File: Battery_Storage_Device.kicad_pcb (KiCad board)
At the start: 4 copper layers, 80 x 75 mm, 130 parts, among them J1 Conn_01x02_Female, J2 Conn_01x07_Male, J3 USB_B_Mini, J4 Barrel_Jack_Switch, J5 Conn_02x03_Odd_Even, K1 EE2-5NU, Q1 MMBT5551L, Q10 BSS84, Q11 BSS84, Q12 BSS138, Q13 BSS138, Q14 BSS84, Q15 BSS138, Q16 BSS84, Q17 BSS138, Q2 MMBT5551L, Q3 Q_PMOS_GDS, Q4 Q_PMOS_GDS, Q5 BSS138, Q6 BSS84, Q7 BSS84, Q8 BSS138, Q9 BSS138, U1 TLV2372, U10 ATmega328P-AU, U11 LM317_SOT-223, U2 TLV2372, U3 DG408DYZ-T, U4 DG408DYZ-T, U5 DG412xY, U6 TLV2372, U7 ADS1220xPW, U8 LM4030-4.096, U9 FT232RL, Y1 ABM3C-16.000MHZ-D4Y-T

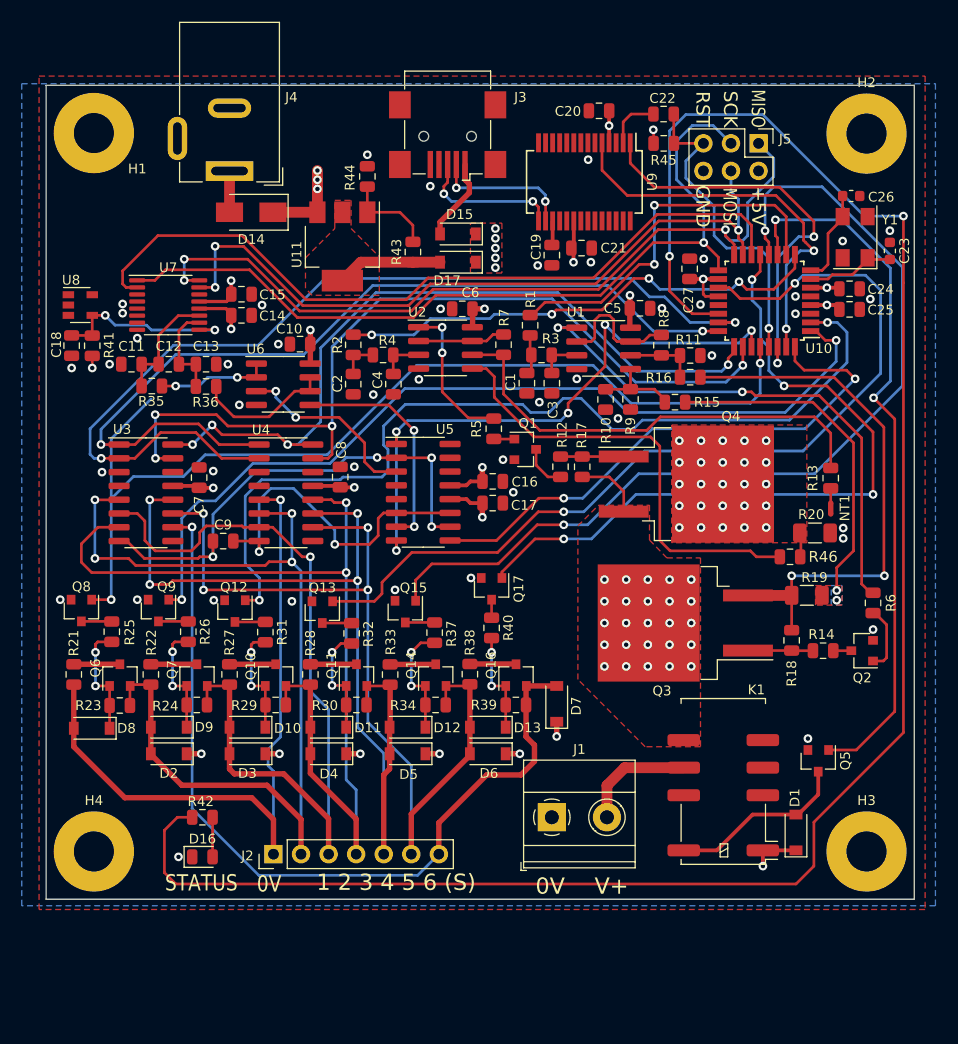
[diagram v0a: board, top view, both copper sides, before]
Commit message: Updates to the AFE power scheme to prevent discharging of the batteries
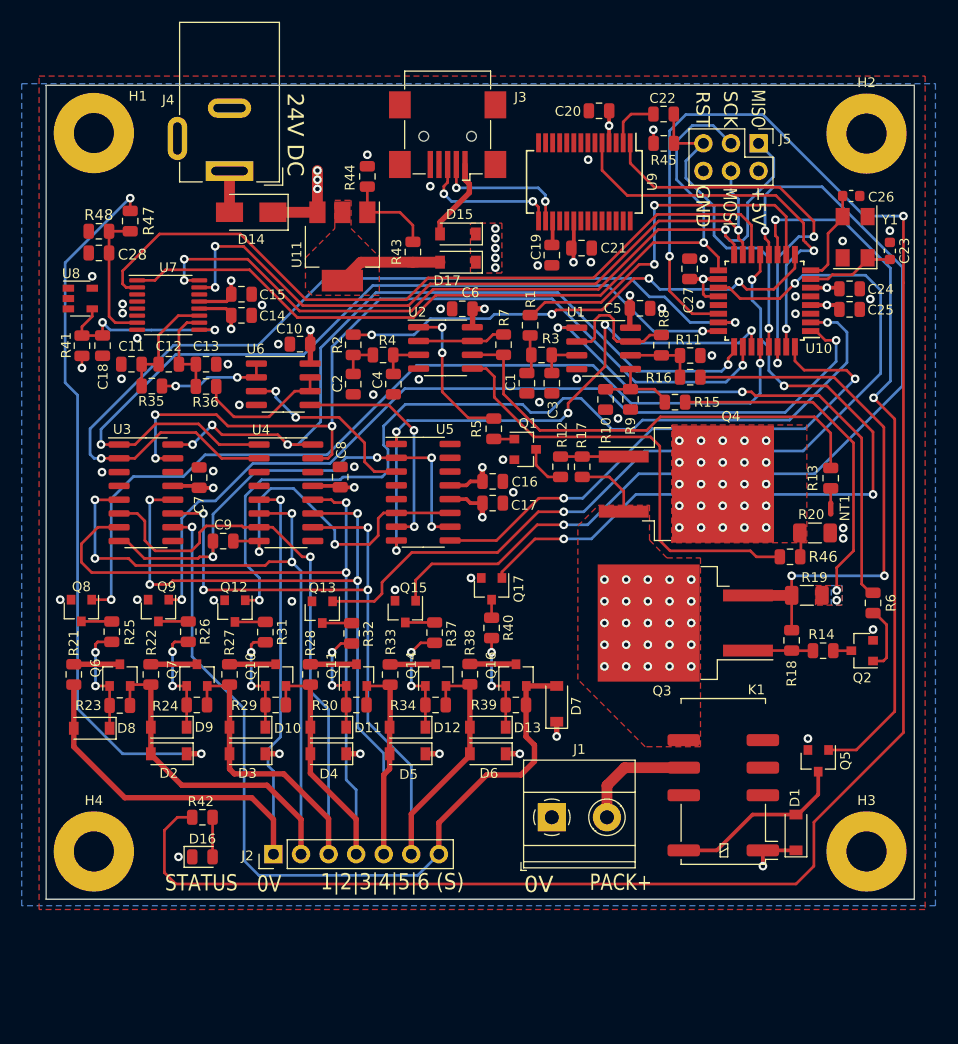
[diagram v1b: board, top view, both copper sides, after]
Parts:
- added C28: 0.1u, Capacitor_SMD:C_0805_2012Metric, F.Cu at (84.9, 65.5)
- added R47: 10M, Resistor_SMD:R_0805_2012Metric, F.Cu at (87.8, 62.5)
- added R48: 2M, Resistor_SMD:R_0805_2012Metric, F.Cu at (84.9, 63.5)
- moved C18 2.85 mm to (85.2, 74.0)
- moved R41 0.95 mm to (83.3, 74.0)
- moved U8 0.60 mm to (83.2, 69.7)
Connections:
- C16 pad 1: +BATT -> +24V
- C7 pad 1: +BATT -> +24V
- C8 pad 1: +BATT -> +24V
- U3 pad 13: +BATT -> +24V
- U4 pad 13: +BATT -> +24V
- U5 pad 13: +BATT -> +24V
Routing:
- net +24V: track 139.0 -> 232.5 mm, vias 5 -> 8
- net Net-(C28-Pad1): track 0.00 -> 12.6 mm
- net /Battery AFE/VC1_BAL: track 92.8 -> 82.1 mm
- net +BATT: track 106.6 -> 105.5 mm, vias 9 -> 7
- net /Battery AFE/VREF: track 17.1 -> 18.1 mm
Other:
- board text added: "1|2|3|4|5|6 (S)"
- board text added: "24V DC"
- board text added: "PACK+"
- board text removed: "1 2 3 4 5 6 (S)"
- board text removed: "V+"

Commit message: New power banana jacks, general updates
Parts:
- added C29: 10n, Capacitor_SMD:C_0805_2012Metric, F.Cu at (83.0, 78.5)
- added D18: 10V, Diode_SMD:D_SOD-123, F.Cu at (150.9, 101.2)
- added D19: 10V, Diode_SMD:D_SOD-123, F.Cu at (127.3, 85.6)
- added D20: LED, LED_SMD:LED_0805_2012Metric, F.Cu at (107.5, 51.7)
- added J6: Conn_01x01_Female, battery-storage-device:banana_jack_right_angle, F.Cu at (125.0, 112.2)
- added R49: 1k, Resistor_SMD:R_0805_2012Metric, F.Cu at (106.8, 55.9)
- added R50: 10M, Resistor_SMD:R_0805_2012Metric, F.Cu at (128.6, 91.9)
- added R51: 2M, Resistor_SMD:R_0805_2012Metric, F.Cu at (83.0, 80.5)
- added R52: 10k, Resistor_SMD:R_0805_2012Metric, F.Cu at (91.8, 63.8)
- added R53: 10k, Resistor_SMD:R_0805_2012Metric, F.Cu at (107.0, 74.0)
- added R54: 10k, Resistor_SMD:R_0805_2012Metric, F.Cu at (149.2, 56.9)
- added TP1: TestPoint, TestPoint:TestPoint_THTPad_D2.0mm_Drill1.0mm, F.Cu at (138.6, 71.5)
- added TP2: TestPoint, TestPoint:TestPoint_THTPad_D2.0mm_Drill1.0mm, F.Cu at (128.3, 80.5)
- added TP3: TestPoint, TestPoint:TestPoint_THTPad_D2.0mm_Drill1.0mm, F.Cu at (133.7, 107.2)
- added TP4: TestPoint, TestPoint:TestPoint_THTPad_D2.0mm_Drill1.0mm, F.Cu at (116.0, 79.2)
- added TP5: TestPoint, TestPoint:TestPoint_THTPad_D2.0mm_Drill1.0mm, F.Cu at (122.7, 72.0)
- added TP6: TestPoint, TestPoint:TestPoint_THTPad_D2.0mm_Drill1.0mm, F.Cu at (87.1, 115.2)
- C1, C2: value 10n -> 0.1u
- C28: value 0.1u -> 10n
- H1, H2, H3, H4: footprint MountingHole:MountingHole_3.7mm_Pad -> MountingHole:MountingHole_2.7mm_M2.5_Pad
- J1: value Conn_01x02_Female -> Conn_01x01_Female; footprint TerminalBlock_Phoenix:TerminalBlock_Phoenix_MKDS-1,5-2-5.08_1x02_P5.08mm_Horizontal -> battery-storage-device:banana_jack_right_angle
- J2: footprint Connector_PinHeader_2.54mm:PinHeader_1x07_P2.54mm_Vertical -> Connector_PinHeader_2.54mm:PinHeader_1x07_P2.54mm_Horizontal
- R17, R18: value 1M -> 100k
- R3, R4: value 100k -> 1M
- moved J1 16.3 mm to (142.0, 112.2)
- moved J2 13.6 mm to (113.5, 126.2), turned to 270 degrees
- moved D1 12.8 mm to (147.4, 106.2), turned to 270 degrees
- moved K1 11.7 mm to (154.1, 113.1)
- moved Q5 9.01 mm to (144.3, 106.4)
- moved H4 6.20 mm to (83.3, 126.7)
- moved H3 6.20 mm to (156.7, 126.7)
- moved D16 5.96 mm to (92.1, 126.6)
- moved R42 5.96 mm to (92.1, 123.0)
- moved D6 5.72 mm to (116.2, 115.2), turned to 270 degrees
- moved Q17 4.51 mm to (125.3, 95.0)
- moved R40 3.98 mm to (121.5, 96.0), turned to 0 degrees
- moved D13 3.81 mm to (120.5, 105.3)
- moved D7 3.81 mm to (126.8, 103.2)
- moved Q16 3.81 mm to (123.0, 100.5)
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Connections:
- J1 pad 1: GND -> /PACK_HI
- J2 pad 1: /Battery AFE/VC0 -> /Battery AFE/VC6
- J2 pad 2: /Battery AFE/VC1 -> /Battery AFE/VC5
- J2 pad 3: /Battery AFE/VC2 -> /Battery AFE/VC4
- J2 pad 5: /Battery AFE/VC4 -> /Battery AFE/VC2
- J2 pad 6: /Battery AFE/VC5 -> /Battery AFE/VC1
- J2 pad 7: /Battery AFE/VC6 -> /Battery AFE/VC0
- U7 pad 6: GND -> Net-(C29-Pad1)
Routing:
- net Net-(C29-Pad1): track 0.00 -> 73.2 mm, vias 0 -> 2
- net GND: track 0.07 -> 19.1 mm, vias 45 -> 53
- net /SRC_SINK: track 6.24 -> 21.1 mm, vias 25 -> 29
- net /Battery AFE/VC5: track 83.8 -> 98.3 mm
- net /PACK_HI: track 10.7 -> 24.0 mm
- net /Battery AFE/VC4: track 85.6 -> 97.5 mm
- net /Battery AFE/VC6: track 78.0 -> 89.9 mm
- net +BATT: track 105.5 -> 117.1 mm, vias 7 -> 6
- net /Battery AFE/VC3: track 88.0 -> 97.9 mm
- net /Battery AFE/VC5_BAL: track 86.8 -> 95.7 mm
- net /Battery AFE/VC4_BAL: track 84.2 -> 92.8 mm
- net /Microcontroller/PWM_SRC: track 34.9 -> 43.1 mm, vias 2 -> 4
- net /Battery AFE/VC2: track 76.8 -> 83.5 mm
- net /Battery AFE/VC1: track 90.7 -> 96.8 mm
- net Net-(C4-Pad1): track 4.10 -> 9.79 mm
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- added copper zone on B.Cu, net /SRC_SINK
- added copper zone on In1.Cu, net /SRC_SINK
- added copper zone on B.Cu, net Net-(D17-Pad2)
- added copper zone on F.Cu, net Net-(D18-Pad1)
- added copper zone on B.Cu, net Net-(Q4-Pad2)
- added copper zone on In1.Cu, net Net-(Q4-Pad2)
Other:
- board size 80 x 75 mm -> 80 x 80 mm
- board text added: "Adam Cordingley"
- board text added: "Li-Ion/LiPo Battery Storage Charger Rev 1.0"
